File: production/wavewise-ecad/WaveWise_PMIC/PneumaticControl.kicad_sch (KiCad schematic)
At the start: 8 parts, among them K2 Relay_SPST-NO, Q2 2N2219, U1 Pololu_DRV8711_Motor_Driver

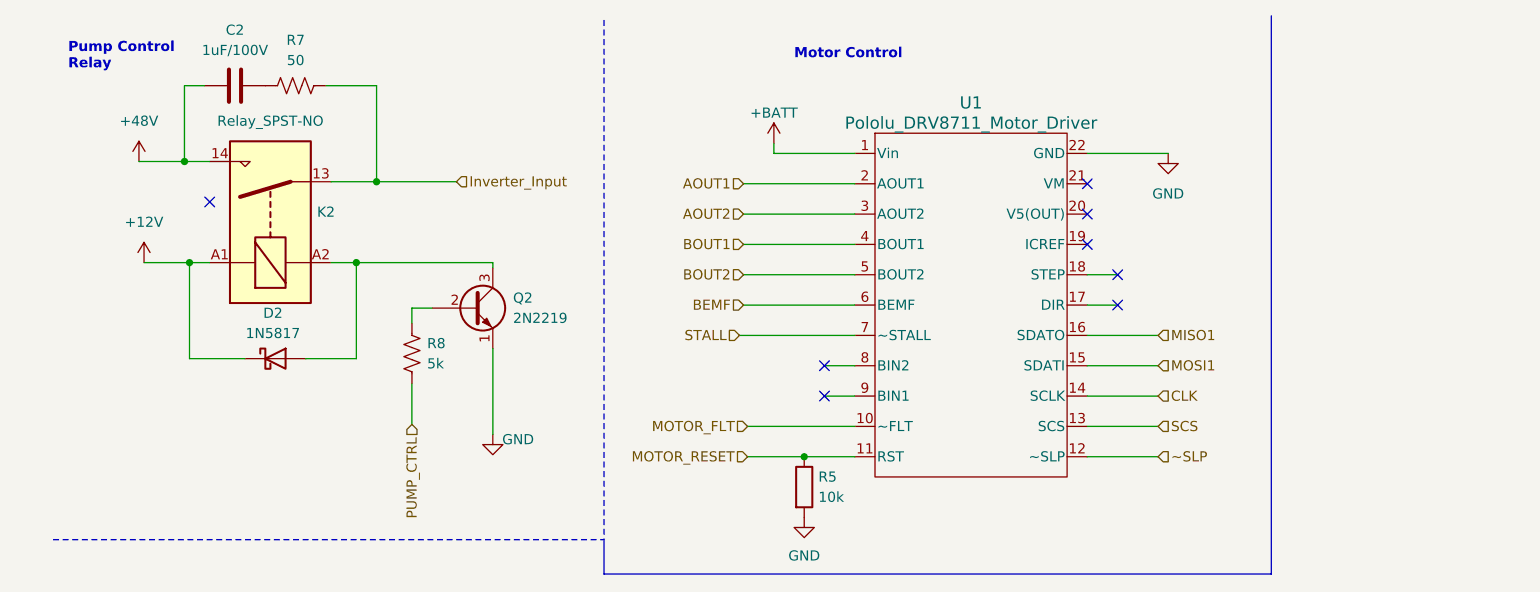
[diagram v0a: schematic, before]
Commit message: added most footprints still need polulu footprint
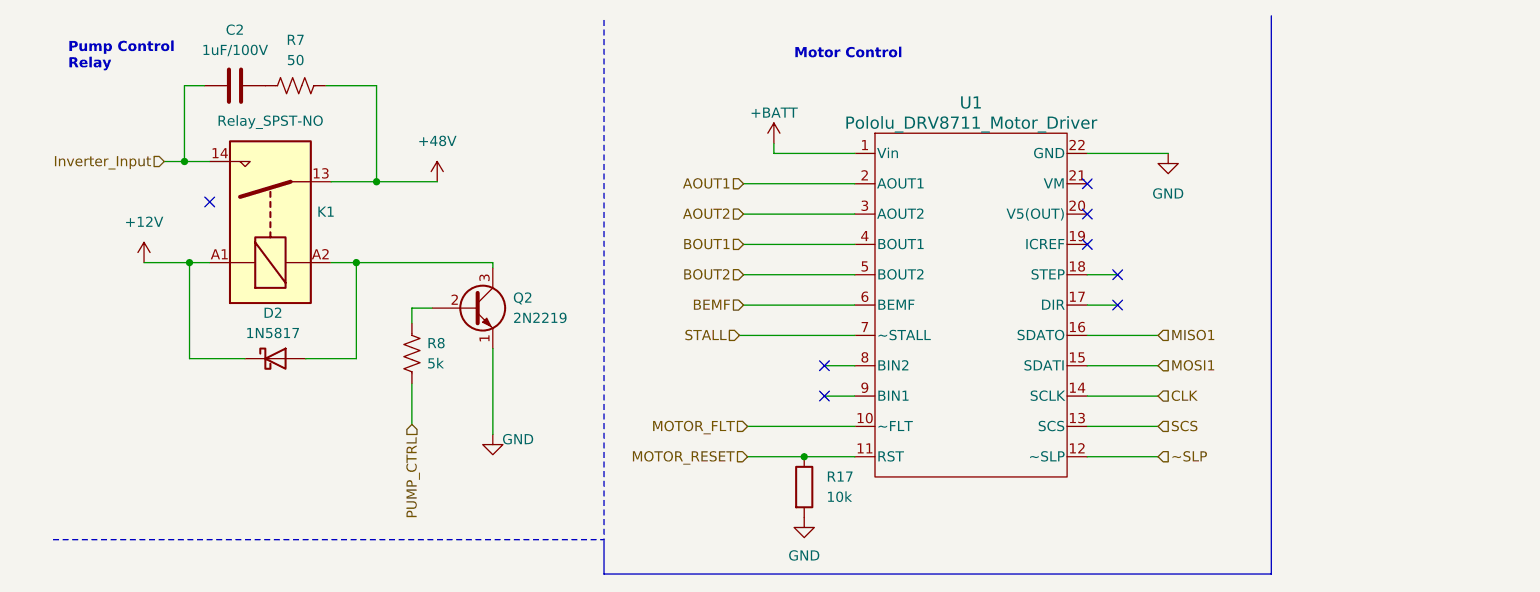
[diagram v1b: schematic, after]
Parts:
- C2: footprint (none) -> Capacitor_THT:C_Disc_D5.0mm_W2.5mm_P5.00mm
- K1: renamed from K2; footprint (none) -> Relay_THT:Relay_SPDT_Finder_36.11
- R8: footprint (none) -> Resistor_SMD:R_0805_2012Metric_Pad1.20x1.40mm_HandSolder
- renumbered R5 to R17
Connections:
- net +48V: now also K1.13, R7.2; no longer C2.2, K1.14
- net Inverter_Input: now also C2.2, K1.14; no longer K1.13, R7.2
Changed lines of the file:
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@@
 (kicad_sch (version 20230121) (generator eeschema)
   (paper "A4")
+  (junction (at 53.975 33.02) (diameter 0) (color 0 0 0 0)
+  )
   (junction (at 29.845 30.48) (diameter 0) (color 0 0 0 0)
   )
   (junction (at 107.696 67.564) (diameter 0) (color 0 0 0 0)
-  )
-  (junction (at 53.975 33.02) (diameter 0) (color 0 0 0 0)
   )
   (junction (at 51.435 43.18) (diameter 0) (color 0 0 0 0)
@@
     (stroke (width 0) (type default))
   )
-  (wire (pts (xy 53.975 33.02) (xy 64.008 33.02))
-    (stroke (width 0) (type default))
-  )
   (wire (pts (xy 143.256 63.754) (xy 152.146 63.754))
+    (stroke (width 0) (type default))
+  )
+  (wire (pts (xy 53.975 33.02) (xy 61.595 33.02))
     (stroke (width 0) (type default))
   )
@@
     (stroke (width 0) (type default))
   )
-  (wire (pts (xy 24.13 30.48) (xy 29.845 30.48))
-    (stroke (width 0) (type default))
-  )
   (wire (pts (xy 143.256 44.704) (xy 147.066 44.704))
     (stroke (width 0) (type default))
@@
     (stroke (width 0) (type default))
   )
+  (wire (pts (xy 29.845 30.48) (xy 27.305 30.48))
+    (stroke (width 0) (type default))
+  )
   (wire (pts (xy 29.845 30.48) (xy 33.02 30.48))
     (stroke (width 0) (type default))
@@
     (effects (font (size 1.27 1.27)) (justify right))
   )
+  (hierarchical_label "Inverter_Input" (shape input) (at 27.305 30.48 180) (fields_autoplaced)
+    (effects (font (size 1.27 1.27)) (justify right))
+  )
   (hierarchical_label "BOUT2" (shape input) (at 100.076 44.704 180) (fields_autoplaced)
     (effects (font (size 1.27 1.27)) (justify right))
@@
   )
   (hierarchical_label "MOSI1" (shape input) (at 152.146 56.134 0) (fields_autoplaced)
-    (effects (font (size 1.27 1.27)) (justify left))
-  )
-  (hierarchical_label "Inverter_Input" (shape input) (at 64.008 33.02 0) (fields_autoplaced)
     (effects (font (size 1.27 1.27)) (justify left))
   )
@@
     )
   )
-  (symbol (lib_id "power:+48V") (at 24.13 30.48 0) (unit 1)
-    (in_bom yes) (on_board yes) (dnp no) (fields_autoplaced)
-    (property "Reference" "#PWR05" (at 24.13 34.29 0)
-      (effects (font (size 1.27 1.27)) hide)
-    )
-    (property "Value" "+48V" (at 24.13 25.4 0)
-      (effects (font (size 1.27 1.27)))
-    )
-    (property "Footprint" "" (at 24.13 30.48 0)
-      (effects (font (size 1.27 1.27)) hide)
-    )
-    (property "Datasheet" "" (at 24.13 30.48 0)
-      (effects (font (size 1.27 1.27)) hide)
-    )
-    (pin "1")
-    (instances
-      (project "WaveWise_PMIC"
-        (path "/8343c01b-8940-4cb8-a17d-91fd7fb1cccd/9401b93a-998f-4185-ba4a-cb0793660d5a"
-          (reference "#PWR05") (unit 1)
-        )
-      )
-    )
-  )
   (symbol (lib_id "power:GND") (at 68.58 64.77 0) (unit 1)
     (in_bom yes) (on_board yes) (dnp no)
@@
         (path "/ac491dca-bdaf-4a2e-a85e-04a34a1180ec"
           (reference "#PWR014") (unit 1)
+        )
+      )
+    )
+  )
+  (symbol (lib_id "power:+48V") (at 61.595 33.02 0) (unit 1)
+    (in_bom yes) (on_board yes) (dnp no) (fields_autoplaced)
+    (property "Reference" "#PWR02" (at 61.595 36.83 0)
+      (effects (font (size 1.27 1.27)) hide)
+    )
+    (property "Value" "+48V" (at 61.595 27.94 0)
+      (effects (font (size 1.27 1.27)))
+    )
+    (property "Footprint" "" (at 61.595 33.02 0)
+      (effects (font (size 1.27 1.27)) hide)
+    )
+    (property "Datasheet" "" (at 61.595 33.02 0)
+      (effects (font (size 1.27 1.27)) hide)
+    )
+    (pin "1")
+    (instances
+      (project "WaveWise_PMIC"
+        (path "/8343c01b-8940-4cb8-a17d-91fd7fb1cccd/9401b93a-998f-4185-ba4a-cb0793660d5a"
+          (reference "#PWR02") (unit 1)
         )
       )
@@
       (effects (font (size 1.27 1.27)) (justify right))
     )
-    (property "Footprint" "" (at 57.404 54.356 90)
+    (property "Footprint" "Resistor_SMD:R_0805_2012Metric_Pad1.20x1.40mm_HandSolder" (at 57.404 54.356 90)
       (effects (font (size 1.27 1.27)) hide)
     )
@@
   (symbol (lib_id "Relay:Relay_SPST-NO") (at 40.64 38.1 90) (unit 1)
     (in_bom yes) (on_board yes) (dnp no)
-    (property "Reference" "K2" (at 47.625 36.83 90)
+    (property "Reference" "K1" (at 47.625 36.83 90)
       (effects (font (size 1.27 1.27)))
     )
@@
       (effects (font (size 1.27 1.27)))
     )
-    (property "Footprint" "" (at 41.91 26.67 0)
+    (property "Footprint" "Relay_THT:Relay_SPDT_Finder_36.11" (at 41.91 26.67 0)
       (effects (font (size 1.27 1.27)) (justify left) hide)
     )
@@
       (project "WaveWise_PMIC"
         (path "/8343c01b-8940-4cb8-a17d-91fd7fb1cccd/9401b93a-998f-4185-ba4a-cb0793660d5a"
-          (reference "K2") (unit 1)
+          (reference "K1") (unit 1)
         )
       )
@@
   (symbol (lib_id "Device:R") (at 107.696 71.374 0) (unit 1)
     (in_bom yes) (on_board yes) (dnp no) (fields_autoplaced)
-    (property "Reference" "R5" (at 109.474 70.104 0)
+    (property "Reference" "R17" (at 110.49 70.104 0)
       (effects (font (size 1.27 1.27)) (justify left))
     )
-    (property "Value" "10k" (at 109.474 72.644 0)
+    (property "Value" "10k" (at 110.49 72.644 0)
       (effects (font (size 1.27 1.27)) (justify left))
     )
@@
       (project "WaveWise_PMIC"
         (path "/8343c01b-8940-4cb8-a17d-91fd7fb1cccd/9401b93a-998f-4185-ba4a-cb0793660d5a"
-          (reference "R5") (unit 1)
+          (reference "R17") (unit 1)
         )
       )
@@
       (effects (font (size 1.27 1.27)))
     )
-    (property "Footprint" "" (at 32.385 21.9202 0)
-      (effects (font (size 1.27 1.27)) hide)
-    )
+    (property "Footprint" "Capacitor_THT:C_Disc_D5.0mm_W2.5mm_P5.00mm" (at 32.385 21.9202 0)
+      (effects (font (size 1.27 1.27)) hide)
+    )

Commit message: More stuff done to PCB Added polulu
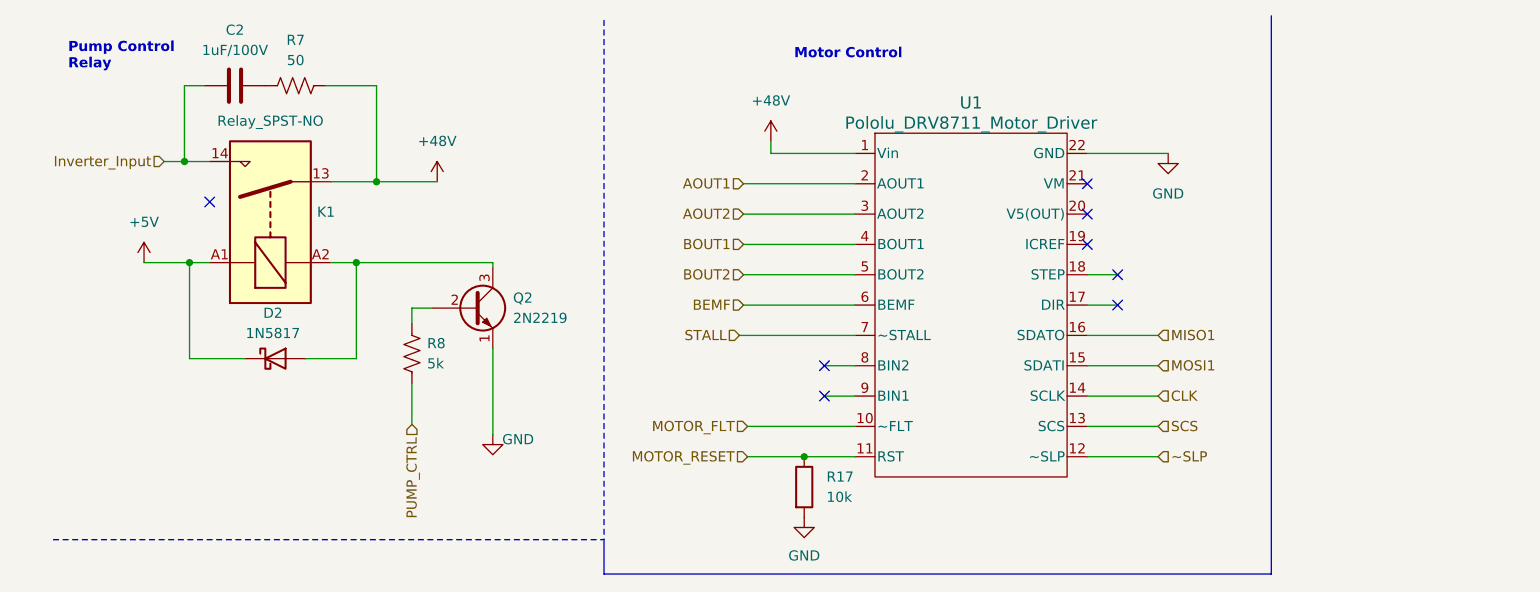
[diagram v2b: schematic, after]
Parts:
- U1: footprint Wavewise Footprints UnChecked:POLOLU_36v4 -> Unchecked:POLOLU_36v4
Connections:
- net +BATT is gone; now on net +48V: U1.1 (Vin)
- net +12V renamed +5V
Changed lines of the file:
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@@
     (stroke (width 0) (type default))
   )
-  (wire (pts (xy 103.886 29.464) (xy 114.046 29.464))
+  (wire (pts (xy 103.505 29.464) (xy 114.046 29.464))
     (stroke (width 0) (type default))
   )
@@
     (stroke (width 0) (type default))
   )
-  (wire (pts (xy 103.886 29.464) (xy 103.886 28.194))
+  (wire (pts (xy 103.505 29.464) (xy 103.505 27.94))
     (stroke (width 0) (type default))
   )
@@
     (effects (font (size 1.27 1.27)) (justify right))
   )
-  (symbol (lib_id "power:+12V") (at 24.765 43.18 0) (unit 1)
-    (in_bom yes) (on_board yes) (dnp no) (fields_autoplaced)
-    (property "Reference" "#PWR07" (at 24.765 46.99 0)
-      (effects (font (size 1.27 1.27)) hide)
-    )
-    (property "Value" "+12V" (at 24.765 38.1 0)
-      (effects (font (size 1.27 1.27)))
-    )
-    (property "Footprint" "" (at 24.765 43.18 0)
-      (effects (font (size 1.27 1.27)) hide)
-    )
-    (property "Datasheet" "" (at 24.765 43.18 0)
-      (effects (font (size 1.27 1.27)) hide)
-    )
-    (pin "1")
-    (instances
-      (project "WaveWise_PMIC"
-        (path "/8343c01b-8940-4cb8-a17d-91fd7fb1cccd/9401b93a-998f-4185-ba4a-cb0793660d5a"
-          (reference "#PWR07") (unit 1)
+  (symbol (lib_id "power:+48V") (at 103.505 27.94 0) (unit 1)
+    (in_bom yes) (on_board yes) (dnp no) (fields_autoplaced)
+    (property "Reference" "#PWR011" (at 103.505 31.75 0)
+      (effects (font (size 1.27 1.27)) hide)
+    )
+    (property "Value" "+48V" (at 103.505 22.86 0)
+      (effects (font (size 1.27 1.27)))
+    )
+    (property "Footprint" "" (at 103.505 27.94 0)
+      (effects (font (size 1.27 1.27)) hide)
+    )
+    (property "Datasheet" "" (at 103.505 27.94 0)
+      (effects (font (size 1.27 1.27)) hide)
+    )
+    (pin "1")
+    (instances
+      (project "WaveWise_PMIC"
+        (path "/8343c01b-8940-4cb8-a17d-91fd7fb1cccd/9401b93a-998f-4185-ba4a-cb0793660d5a"
+          (reference "#PWR011") (unit 1)
         )
       )
@@
         (path "/8343c01b-8940-4cb8-a17d-91fd7fb1cccd/9401b93a-998f-4185-ba4a-cb0793660d5a"
           (reference "#PWR032") (unit 1)
-        )
-      )
-    )
-  )
-  (symbol (lib_id "power:+BATT") (at 103.886 28.194 0) (unit 1)
-    (in_bom yes) (on_board yes) (dnp no) (fields_autoplaced)
-    (property "Reference" "#PWR02" (at 103.886 32.004 0)
-      (effects (font (size 1.27 1.27)) hide)
-    )
-    (property "Value" "+BATT" (at 103.886 24.384 0)
-      (effects (font (size 1.27 1.27)))
-    )
-    (property "Footprint" "" (at 103.886 28.194 0)
-      (effects (font (size 1.27 1.27)) hide)
-    )
-    (property "Datasheet" "" (at 103.886 28.194 0)
-      (effects (font (size 1.27 1.27)) hide)
-    )
-    (pin "1")
-    (instances
-      (project "WaveWise_Buoy"
-        (path "/592e9c71-e849-48c7-bbac-58569f6cf8ab"
-          (reference "#PWR02") (unit 1)
-        )
-      )
-      (project "WaveWise_LiftControl"
-        (path "/65aeefed-878a-44c2-92d6-311875571bde"
-          (reference "#PWR04") (unit 1)
-        )
-      )
-      (project "WaveWise_PMIC"
-        (path "/8343c01b-8940-4cb8-a17d-91fd7fb1cccd/9401b93a-998f-4185-ba4a-cb0793660d5a"
-          (reference "#PWR011") (unit 1)
-        )
-      )
-      (project "WaveWise_Buoy"
-        (path "/ac491dca-bdaf-4a2e-a85e-04a34a1180ec"
-          (reference "#PWR013") (unit 1)
         )
       )
@@
       (effects (font (size 1.524 1.524)))
     )
-    (property "Footprint" "Wavewise Footprints UnChecked:POLOLU_36v4" (at 106.426 24.384 0)
+    (property "Footprint" "Unchecked:POLOLU_36v4" (at 106.426 24.384 0)
       (effects (font (size 1.27 1.27) italic) hide)
     )
@@
         )
       )
+    )
+  )
+  (symbol (lib_id "power:+5V") (at 24.765 43.18 0) (unit 1)
+    (in_bom yes) (on_board yes) (dnp no) (fields_autoplaced)
+    (property "Reference" "#PWR07" (at 24.765 46.99 0)
+      (effects (font (size 1.27 1.27)) hide)
+    )
+    (property "Value" "+5V" (at 24.765 38.1 0)
+      (effects (font (size 1.27 1.27)))
+    )
+    (property "Footprint" "" (at 24.765 43.18 0)
+      (effects (font (size 1.27 1.27)) hide)
+    )
+    (property "Datasheet" "" (at 24.765 43.18 0)
+      (effects (font (size 1.27 1.27)) hide)
+    )
+    (pin "1")
+    (instances
+      (project "WaveWise_PMIC"
+        (path "/8343c01b-8940-4cb8-a17d-91fd7fb1cccd/9401b93a-998f-4185-ba4a-cb0793660d5a"
+          (reference "#PWR07") (unit 1)
+        )
+      )

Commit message: Prelim board layout
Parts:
- removed K1: Relay_SPST-NO, Relay_THT:Relay_SPDT_Finder_36.11, symbol Relay:Relay_SPST-NO
- added K1: AWHSH105D00G, Unchecked:AWHSH105D00G, symbol AWHSH105D00G:AWHSH105D00G
- added R14, R24: 0, Resistor_SMD:R_0805_2012Metric, symbol Device:R
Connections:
- net +48V: now also K1.2
- net +5V: now also K1.5, R14.2
- net Inverter_Input: now also K1.3
- net at D2.2 (A), Q2.3 (C): now also K1.1
- net DIR/AIN2: now reaches U1.17 (DIR)
- net STEP/AIN1: now reaches U1.18 (STEP)
- net ICREF: now reaches U1.19 (ICREF)
- net ICREF: now also R14.1, R24.1
- net CLK renamed SCLK
- net MISO1 renamed SDATO
- net MOSI1 renamed SDATI
- new net +3.3V: R24.2
- no-connect marks 8 -> 4
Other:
- moved on the sheet: C2, D2, Q2, R17, R7, R8, U1
